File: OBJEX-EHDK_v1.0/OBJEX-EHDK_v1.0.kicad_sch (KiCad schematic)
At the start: 0 parts

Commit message: Battery Connectors & Battery LVL circuits
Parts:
- added D?: 1N4148WS, Diode_SMD:D_SOD-323, symbol Diode:1N4002
- added U?: nRF52840, Package_DFN_QFN:Nordic_AQFN-73-1EP_7x7mm_P0.5mm, symbol MCU_Nordic:nRF52840
- added U? (x2): KXOB25-03X4F-TR, KXOB25-03X4F-TR:KXOB25-03X4F-TR, symbol SolarPanel:KXOB25-03X4F-TR
- added U?: SPV1050TTR, QFN40P300X300X100-21N, symbol SPV1050TTR:SPV1050TTR
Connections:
- new net: U?.A22 (VDD), U?.AD14 (VDD), U?.AD23 (VDD), U?.B1 (VDD), U?.W1 (VDD)
- new net: U?.B7 (VSS), U?.EP (VSS)
- new net: D?.2 (A), U?.1 (VCC)
- new net: U?.1 (VCC), U?.2 (GND)
- new net 4.46V: D?.1 (K)
- new net GND: U?.2 (GND)
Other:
- added sheet BatteryConnectors (Batteryconnectors.kicad_sch)
- added sheet ESP32-C3FH4 (esp32c3fh4.kicad_sch)
- note added: "4.46V @13.50mA"
- note added: "Copyright CERN 2020. This source describes Open Hardware and is licensed under the CERN-OHLW v2 You may redistribute and modify this documentation and make products using it under the terms of the CERN-OHL-W v2 (https:/cern.ch/cern-ohl). This documentation is distributed WITHOUT ANY EXPRESS OR IMPLIED WARRANTY, INCLUDING OF MERCHANTABILITY, SATISFACTORY QUALITY AND FITNESS FOR A PARTICULAR PURPOS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"
- note added: "Energy harvesting DevKit"
- note added: "OBJEX EHDK"

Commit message: update
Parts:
- added C?: 4.7uF, symbol Device:C
- added C? (x4): 12pF, symbol Device:C
- added C?: 0.8pF, symbol Device:C
- added C?: 0.5pF, symbol Device:C
- added L?: 4.7nH, symbol Device:L
- added Y?: 32MHz, symbol Device:Crystal
- added Y?: 32.768kHz, symbol Device:Crystal
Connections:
- net GND: now also U?.B7 (VSS), U?.EP (VSS), U?.F23 (VSS_PA), C?.1, C?.1, C?.2, C?.2, C?.2, C?.2
- net at U?.A23 (XC2): now also C?.2, Y?.2
- net at U?.B24 (XC1): now also C?.2, Y?.1
- net at U?.D2 (XL1/P0.00): now also C?.1, Y?.1
- net at U?.F2 (XL2/P0.01): now also C?.1, Y?.2
- net at U?.H23 (ANT): now also C?.1, L?.2
- new net: C?.1, L?.1
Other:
- moved on the sheet: U?

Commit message: add: nRF52840 & SPV1050TTR
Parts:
- removed C?: 4.7uF, symbol Device:C
- removed C? (x4): 12pF, symbol Device:C
- removed C?: 0.8pF, symbol Device:C
- removed C?: 0.5pF, symbol Device:C
- removed L?: 4.7nH, symbol Device:L
- removed U?: nRF52840, Package_DFN_QFN:Nordic_AQFN-73-1EP_7x7mm_P0.5mm, symbol MCU_Nordic:nRF52840
- removed U?: SPV1050TTR, QFN40P300X300X100-21N, symbol SPV1050TTR:SPV1050TTR
- removed Y?: 32MHz, symbol Device:Crystal
- removed Y?: 32.768kHz, symbol Device:Crystal
- gave numbers to parts that had none: 3
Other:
- added sheet SPV1050TTR (SPV1050TTR.kicad_sch)
- added sheet nRF52840 (nrf52840.kicad_sch)
- moved on the sheet: D1, U1, U2

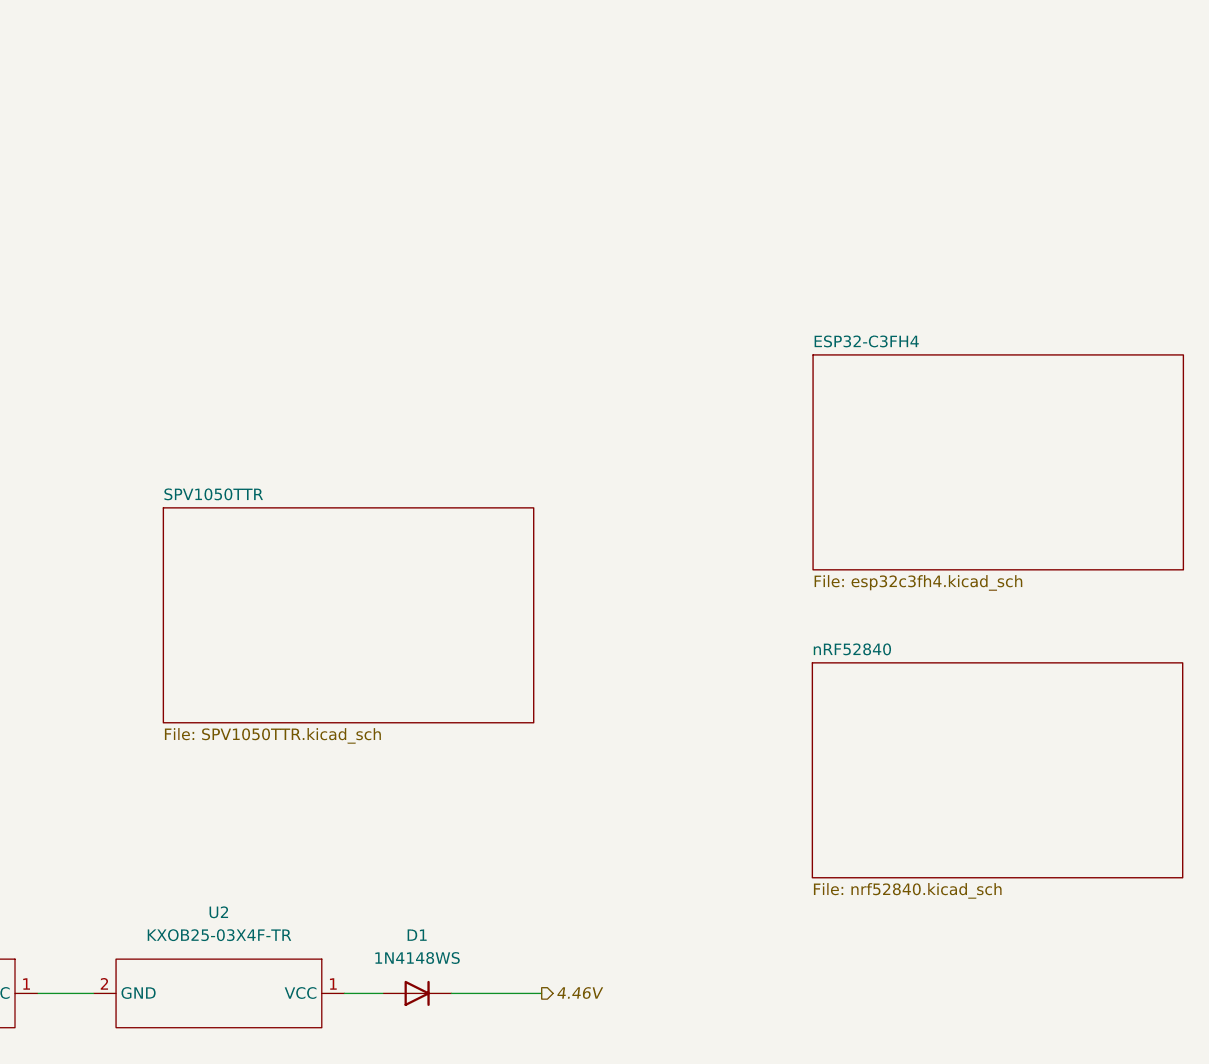
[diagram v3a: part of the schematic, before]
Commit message: add: ADP5091
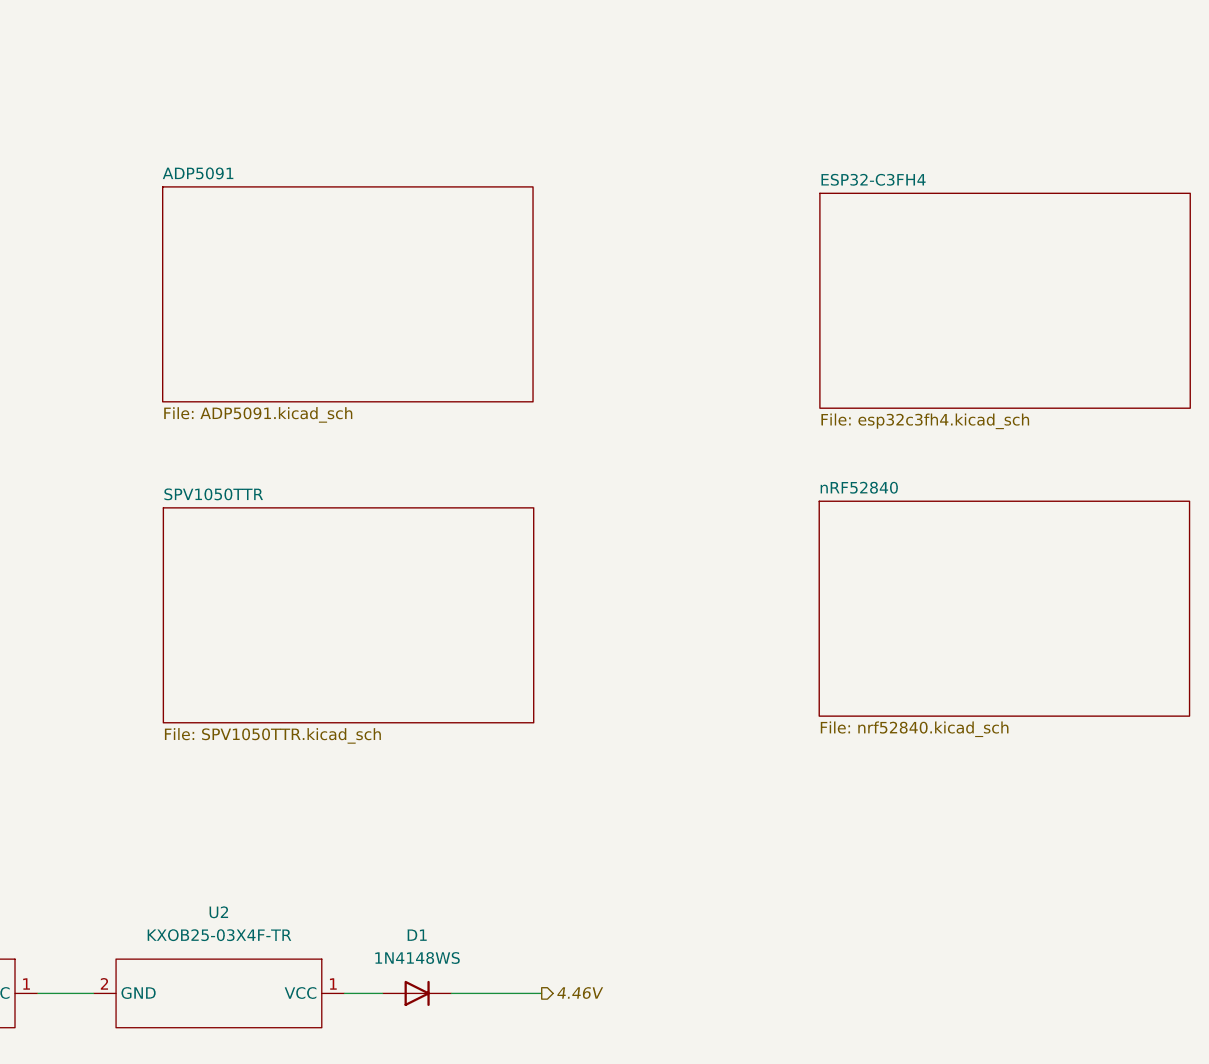
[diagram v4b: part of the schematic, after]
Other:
- added sheet ADP5091 (ADP5091.kicad_sch)

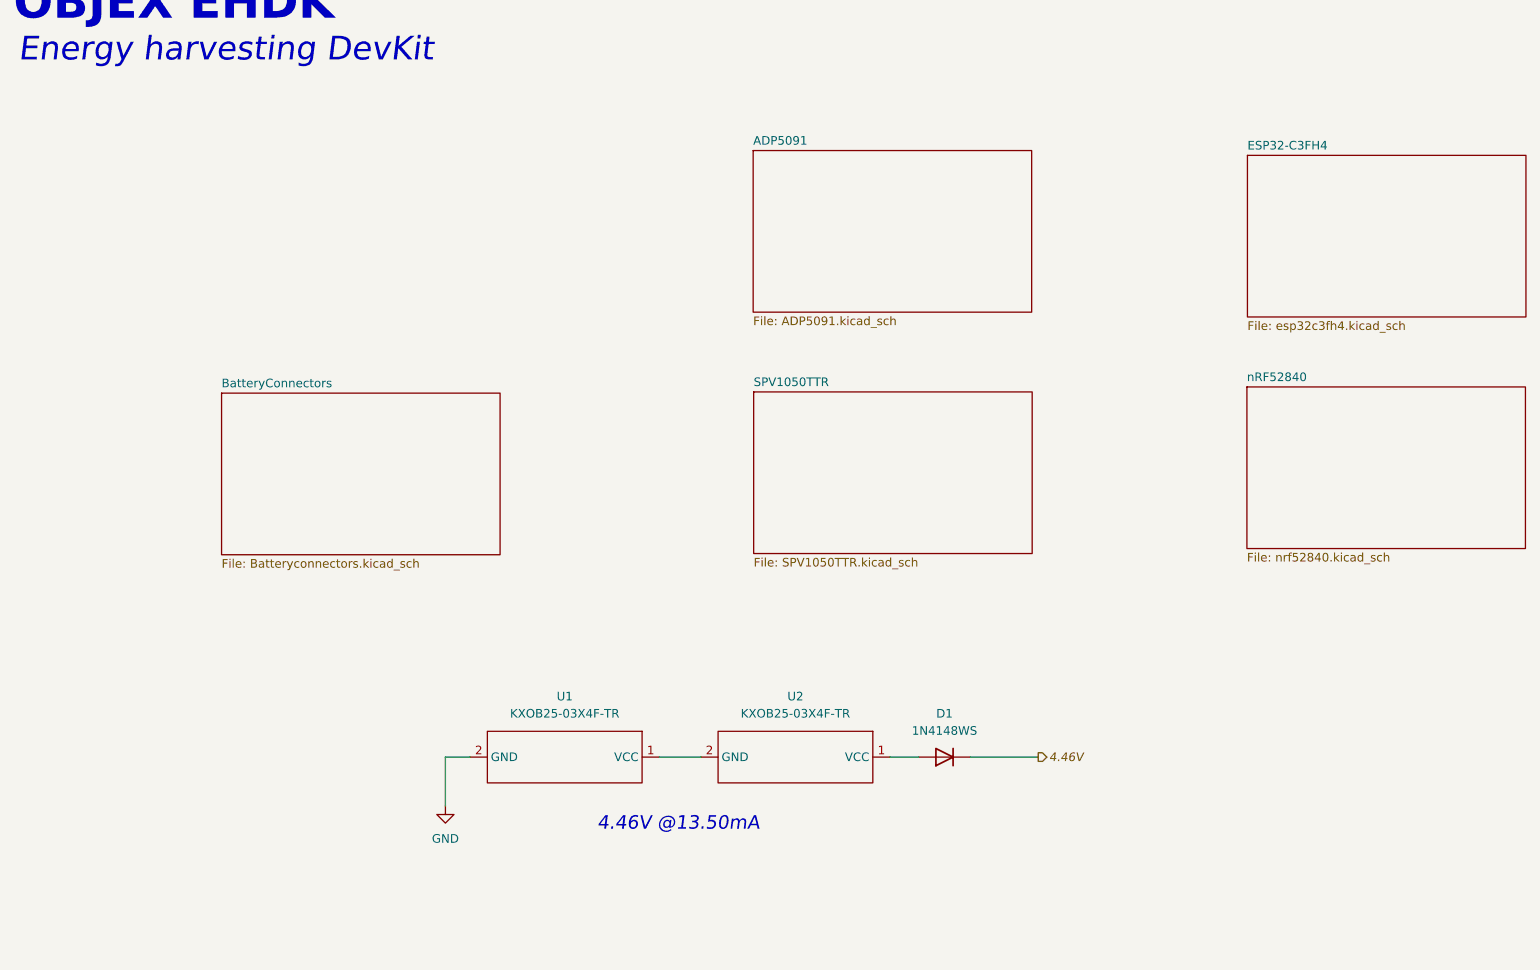
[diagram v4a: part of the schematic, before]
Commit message: Update design, EH ICs & Battery conn
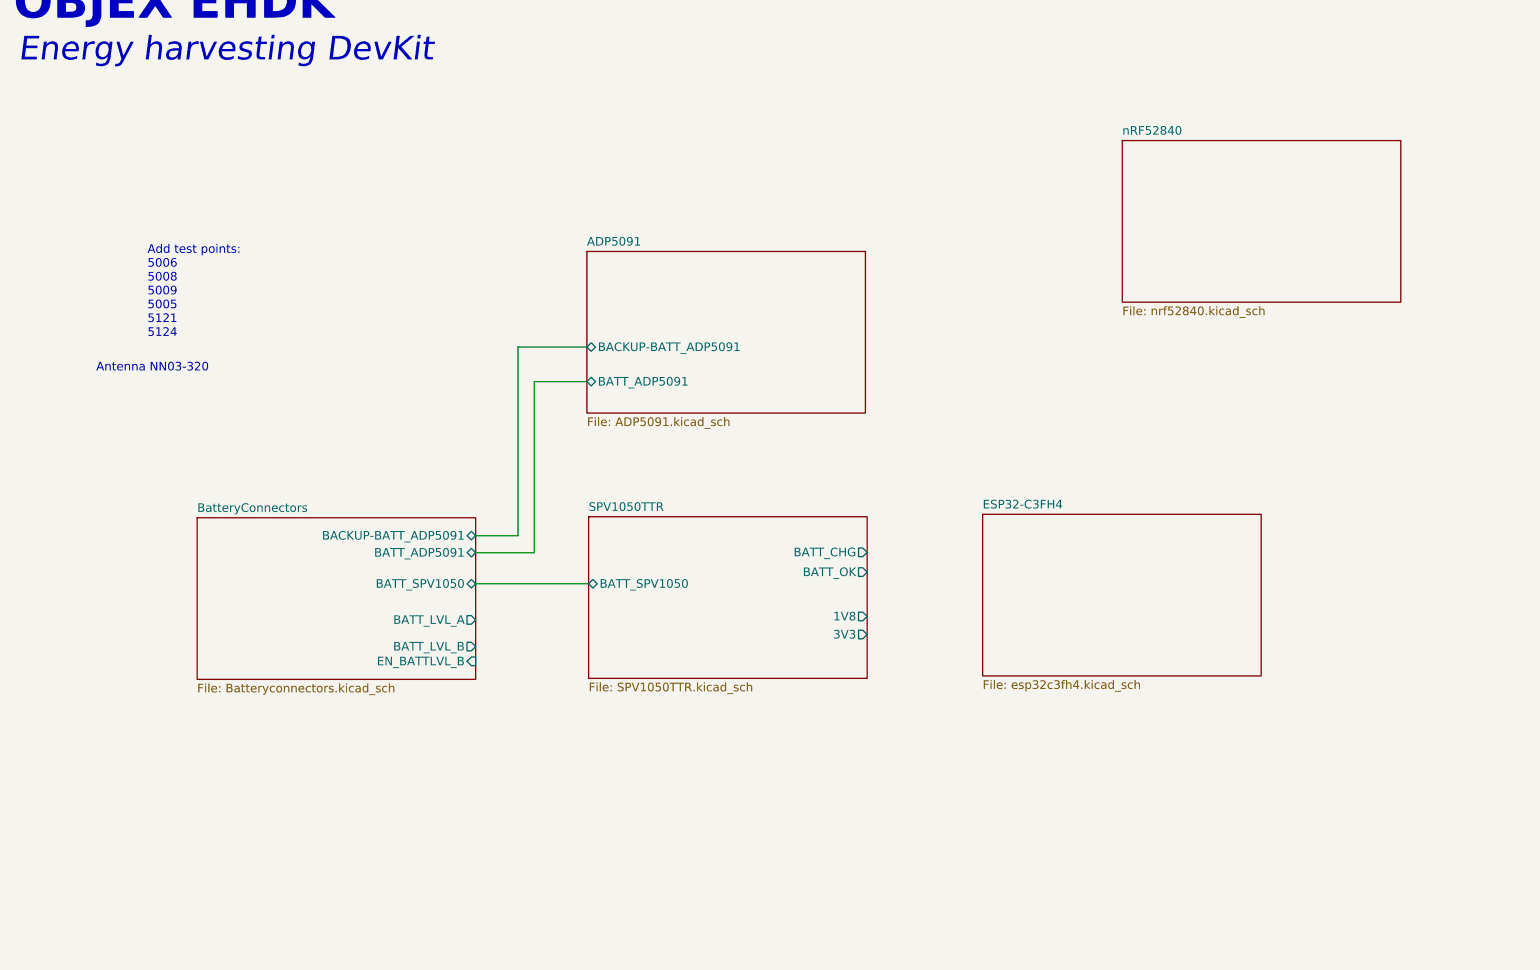
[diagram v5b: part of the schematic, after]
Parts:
- removed D1: 1N4148WS, Diode_SMD:D_SOD-323, symbol Diode:1N4002
- removed U1, U2: KXOB25-03X4F-TR, KXOB25-03X4F-TR:KXOB25-03X4F-TR, symbol SolarPanel:KXOB25-03X4F-TR
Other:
- sheet ADP5091 ports: added BACKUP-BATT_ADP5091, BATT_ADP5091; removed none
- sheet BatteryConnectors ports: added BACKUP-BATT_ADP5091, BATT_ADP5091, BATT_LVL_A, BATT_LVL_B, BATT_SPV1050, EN_BATTLVL_B; removed none
- sheet SPV1050TTR ports: added 1V8, 3V3, BATT_CHG, BATT_OK, BATT_SPV1050; removed none
- note added: "Add test points: 5006 5008 5009 5005 5121 5124"
- note added: "Antenna NN03-320"
- note removed: "4.46V @13.50mA"

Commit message: update
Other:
- note removed: "Add test points: 5006 5008 5009 5005 5121 5124"
- note removed: "Antenna NN03-320"
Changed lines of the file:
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@@
     )
-  )
-  (text "Add test points:\n5006\n5008\n5009\n5005\n5121\n5124\n" (at 36.7284 72.5678 0)
-    (effects (font (size 1.27 1.27)) (justify left bottom))
   )
   (text "OBJEX EHDK" (at 16.9418 26.0096 0)
@@
     (effects (font (size 1.2 1.2)) (justify left bottom))
   )
-  (text "Antenna NN03-320\n" (at 29.1592 77.6732 0)
-    (effects (font (size 1.27 1.27)) (justify left bottom))
-  )
   (text "Energy harvesting DevKit" (at 17.6276 32.004 0)

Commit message: update
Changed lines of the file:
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@@
     )
   )
-  (sheet (at 180.7464 43.307) (size 41.148 23.876) (fields_autoplaced)
+  (sheet (at 221.7674 47.0154) (size 41.148 23.876) (fields_autoplaced)
     (stroke (width 0.1524) (type solid) (color 0 0 0 0))
     (fill (color 0 0 0 0.0000))
-    (property "Sheet name" "nRF52840" (id 0) (at 180.7464 42.5954 0)
+    (property "Sheet name" "nRF52840" (id 0) (at 221.7674 46.3038 0)
       (effects (font (size 1.27 1.27)) (justify left bottom))
     )
-    (property "Sheet file" "nrf52840.kicad_sch" (id 1) (at 180.7464 67.7676 0)
+    (property "Sheet file" "nrf52840.kicad_sch" (id 1) (at 221.7674 71.476 0)
       (effects (font (size 1.27 1.27)) (justify left top))
     )
   )
-  (sheet (at 160.1216 98.5266) (size 41.148 23.876) (fields_autoplaced)
+  (sheet (at 231.0638 112.0394) (size 41.148 23.876) (fields_autoplaced)
     (stroke (width 0.1524) (type solid) (color 0 0 0 0))
     (fill (color 0 0 0 0.0000))
-    (property "Sheet name" "ESP32-C3FH4" (id 0) (at 160.1216 97.815 0)
+    (property "Sheet name" "ESP32-C3FH4" (id 0) (at 231.0638 111.3278 0)
       (effects (font (size 1.27 1.27)) (justify left bottom))
     )
-    (property "Sheet file" "esp32c3fh4.kicad_sch" (id 1) (at 160.1216 122.9872 0)
+    (property "Sheet file" "esp32c3fh4.kicad_sch" (id 1) (at 231.0638 136.5 0)
       (effects (font (size 1.27 1.27)) (justify left top))
     )
@@
       (reference "#PWR?") (unit 1) (value "GND") (footprint "")
     )
+    (path "/1bd0dc3d-4de3-423e-bb17-63b75cf64400/d1ff193b-1c5d-4a55-b19c-cd2950170554"
+      (reference "#PWR?") (unit 1) (value "GND") (footprint "")
+    )
     (path "/c5517dfa-f1e8-47fa-ac1a-f3517e73eb9d/d7168fe5-468d-46b6-9ab4-a5f1711c1e3c"
+      (reference "#PWR?") (unit 1) (value "GND") (footprint "")
+    )
+    (path "/1bd0dc3d-4de3-423e-bb17-63b75cf64400/e77d755b-331b-4e59-a2f7-118f854dc0a5"
       (reference "#PWR?") (unit 1) (value "GND") (footprint "")
     )
@@
       (reference "J2") (unit 1) (value "JST_SM02B") (footprint "KicadLibrary:JST_SM02B-SURS-TF(LF)(SN)")
     )
-    (path "/1bd0dc3d-4de3-423e-bb17-63b75cf64400/d01b8d2b-45dd-42df-b53c-40010e551b16"
-      (reference "J3") (unit 1) (value "SELECT BATT CONN") (footprint "")
-    )
     (path "/1bd0dc3d-4de3-423e-bb17-63b75cf64400/18f5c08b-8854-4a84-b154-fdb39204f21b"
       (reference "J?") (unit 1) (value "Bridge BATT_B") (footprint "")
     )
+    (path "/1bd0dc3d-4de3-423e-bb17-63b75cf64400/1a0c8e9e-4573-412a-a601-446ec9d89bd9"
+      (reference "J?") (unit 1) (value "Conn_LiPoBattery") (footprint "")
+    )
     (path "/a80dc97e-5250-451a-b474-1975e55a6205/2a9cc404-4979-4b85-a0c4-514c25a5dd7b"
       (reference "J?") (unit 1) (value "Conn_01x06") (footprint "")
     )
+    (path "/1bd0dc3d-4de3-423e-bb17-63b75cf64400/444ffcd1-454f-47c9-ab30-84d74ca0e7bc"
+      (reference "J?") (unit 1) (value "JST_SM02B") (footprint "KicadLibrary:JST_SM02B-SURS-TF(LF)(SN)")
+    )
     (path "/1bd0dc3d-4de3-423e-bb17-63b75cf64400/49bd0355-9e50-4dfa-a5f9-49ff838078df"
       (reference "J?") (unit 1) (value "Bridge BATT_A") (footprint "")
     )
-    (path "/1bd0dc3d-4de3-423e-bb17-63b75cf64400/7e8379aa-0b9b-4846-8b10-c28178b0f0d4"
-      (reference "J?") (unit 1) (value "SELECT Vbatt") (footprint "")
-    )
     (path "/1bd0dc3d-4de3-423e-bb17-63b75cf64400/ce069002-67e1-4069-9d6e-8af6305c11e8"
       (reference "J?") (unit 1) (value "BATT / BACKUP") (footprint "")
@@
       (reference "S1") (unit 1) (value "436331045822") (footprint "SamacSys_Parts:436331045822")
     )
-    (path "/1bd0dc3d-4de3-423e-bb17-63b75cf64400/d6d045a5-9e23-4381-acda-f992dccaa96e"
-      (reference "TP1") (unit 1) (value "GND") (footprint "TestPoint:TestPoint_Pad_1.5x1.5mm")
-    )
-    (path "/1bd0dc3d-4de3-423e-bb17-63b75cf64400/10d84c88-d958-42e7-80ee-0dbfa46bf9eb"
-      (reference "TP2") (unit 1) (value "+BATT") (footprint "TestPoint:TestPoint_Pad_1.5x1.5mm")
-    )
     (path "/a80dc97e-5250-451a-b474-1975e55a6205/8e46ddad-6bfa-40af-b04f-edc6699bc195"
